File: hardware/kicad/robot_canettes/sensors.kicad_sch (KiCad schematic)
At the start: 5 parts, among them U2 MPU-6050

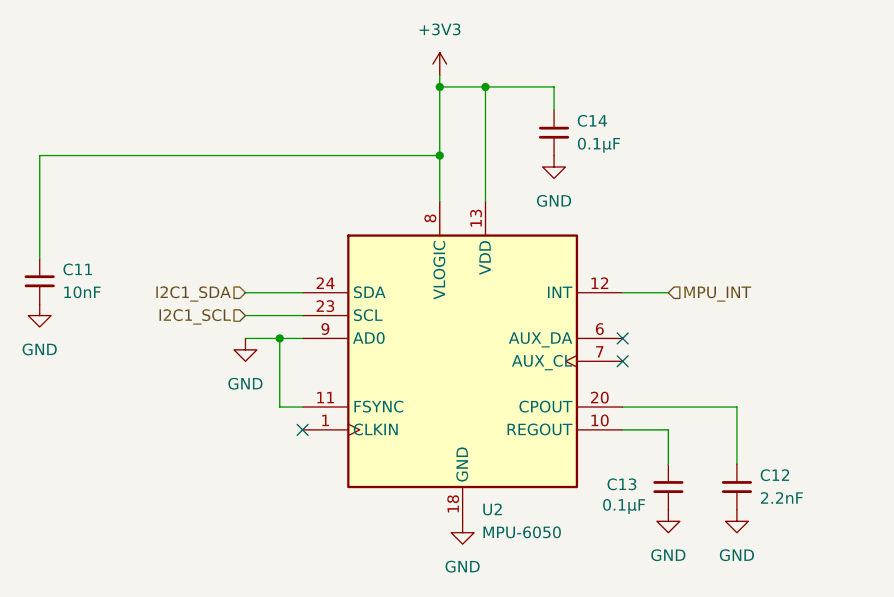
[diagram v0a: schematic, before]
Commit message: MAJ schema MCU/sensors
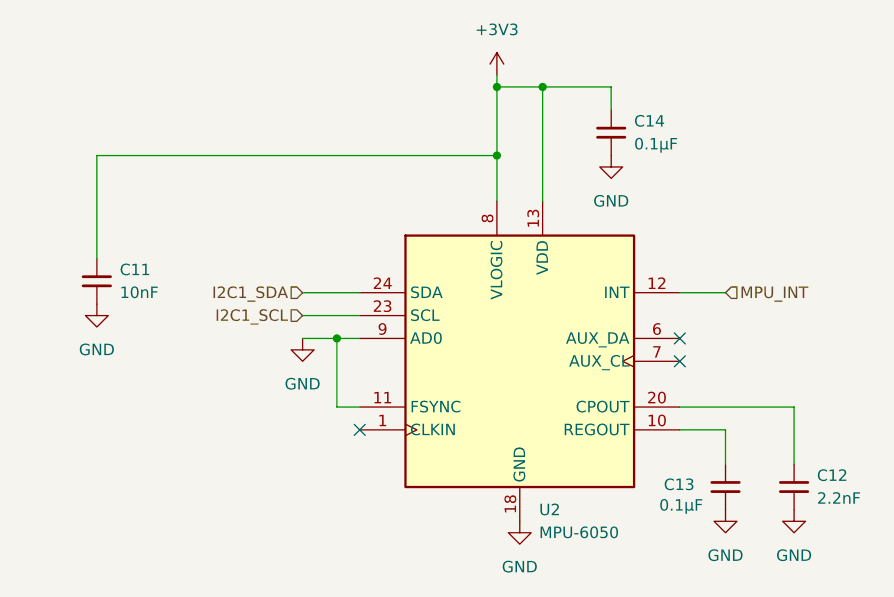
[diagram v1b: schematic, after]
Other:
- moved on the sheet: C11, C12, C13, C14, U2

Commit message: MAJ schema MCU/sensors
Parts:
- C11: JLCPCB PART # (none) -> C15195
- U2: JLCPCB PART # (none) -> C24112
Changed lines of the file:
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@@
+			)
+		)
+		(property "JLCPCB PART #" "C24112"
+			(at 71.12 58.42 0)
+			(hide yes)
+			(show_name no)
+			(do_not_autoplace no)
+			(effects
+				(font
+					(size 1.27 1.27)
+				)
 			)
 		)
@@
 			(hide yes)
 			(show_name no)
+			(do_not_autoplace no)
+			(effects
+				(font
+					(size 1.27 1.27)
+				)
+			)
+		)
+		(property "JLCPCB PART #" "C15195"
+			(at 24.13 49.53 0)
+			(hide yes)
+			(show_name no)

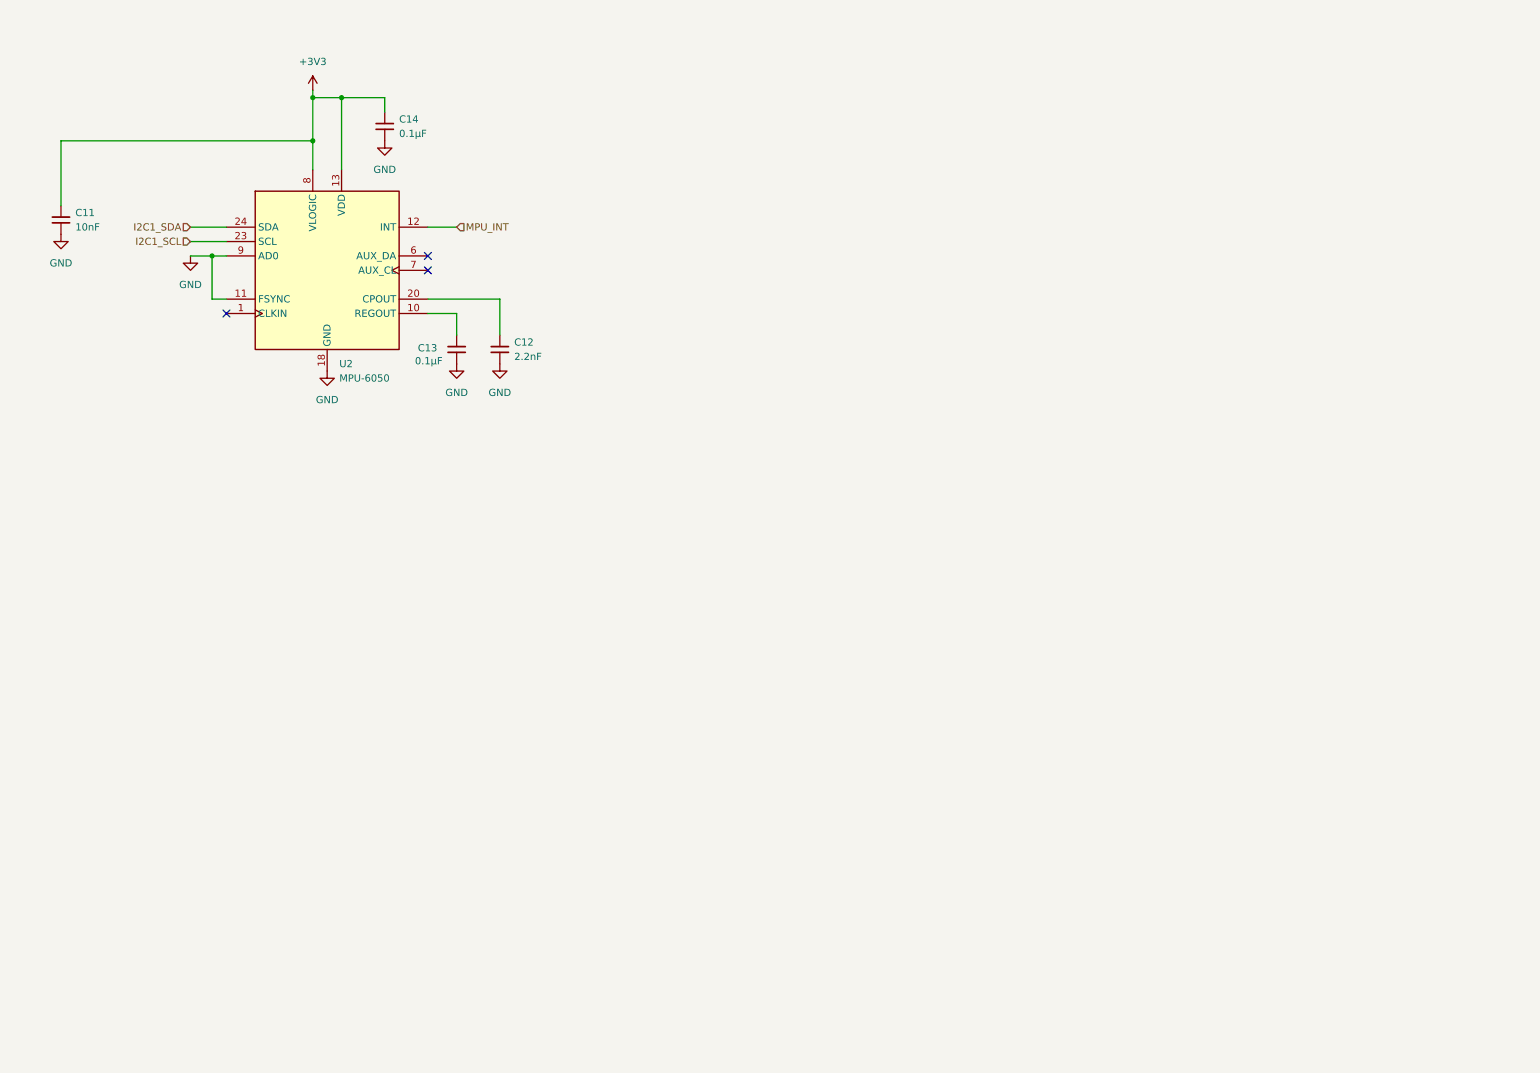
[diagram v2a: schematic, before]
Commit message: MAJ connecteur TOF2 (J10) et resistances pull-up
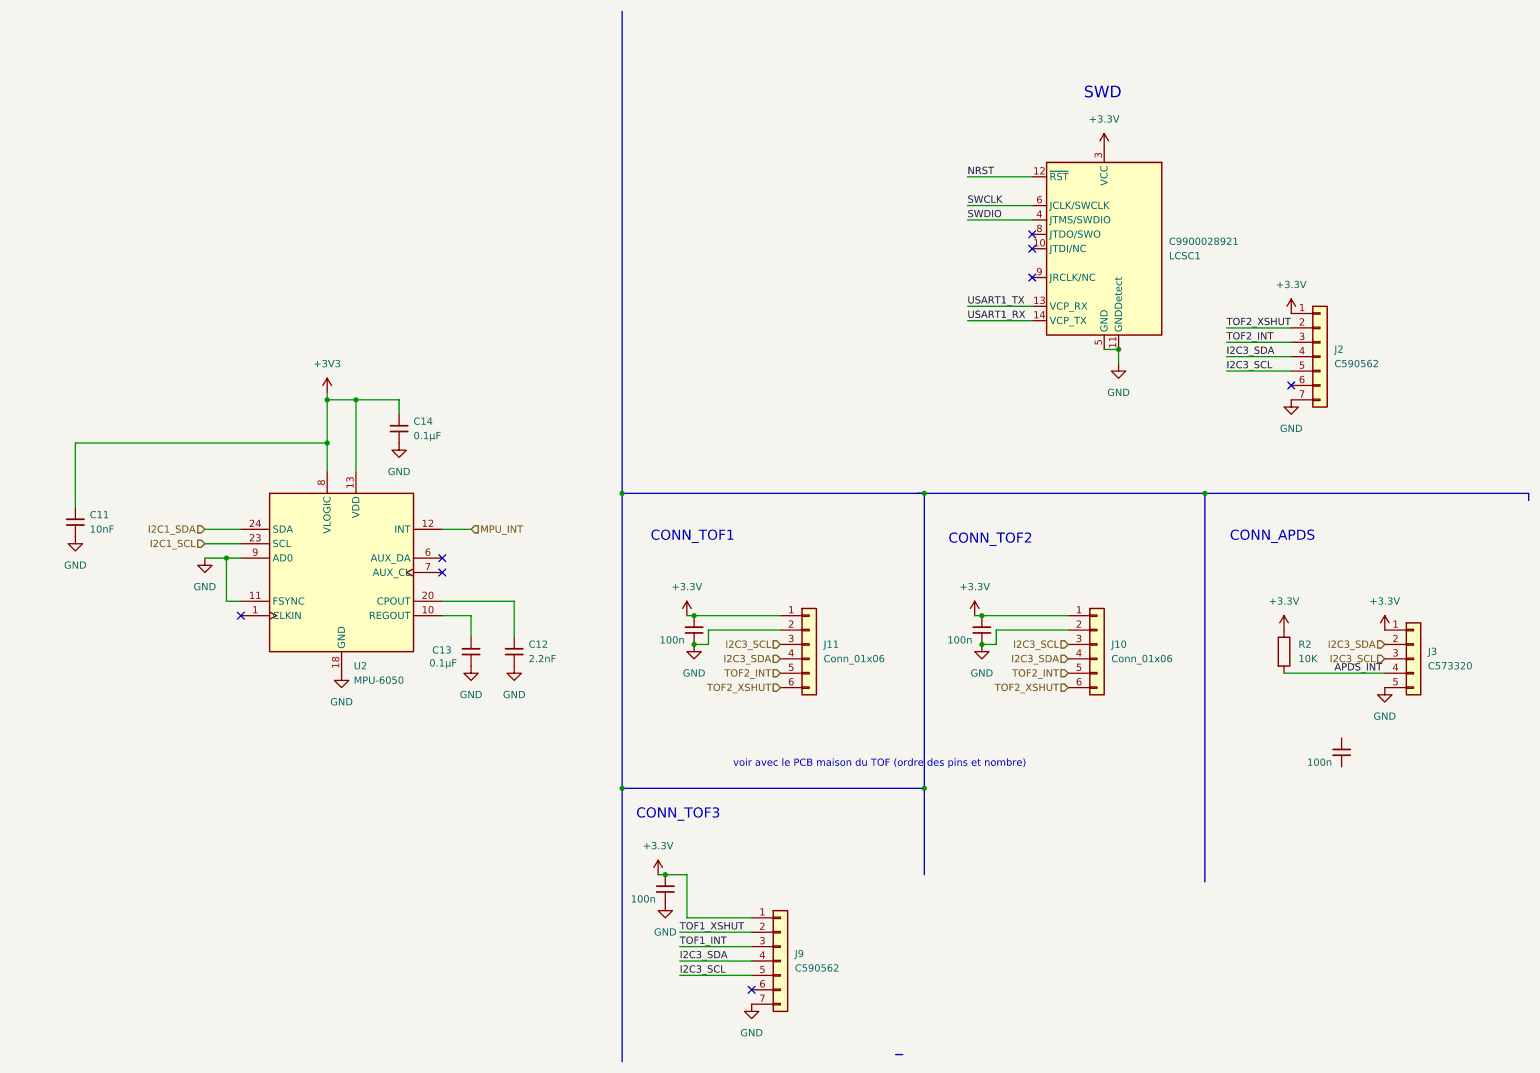
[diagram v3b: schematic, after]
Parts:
- added C36, C38, C39, C40: 100n, symbol Device:C_Small
- added J10, J11: Conn_01x06, symbol Connector_Generic:Conn_01x06
- added J2, J9: C590562, symbol Connector_Generic:Conn_01x07
- added J3: C573320, symbol Connector_Generic:Conn_01x05
- added LCSC1: C9900028921, Package_TO_SOT_SMD:TO-252-2, symbol Connector:Conn_ST_STDC14
- added R2: 10K, symbol Device:R
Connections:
- net GND: now also C36.2, C39.2, C40.2, J10.2 (Pin_2), J11.2 (Pin_2), J2.7 (Pin_7), J3.5 (Pin_5), J9.7 (Pin_7), LCSC1.11 (GNDDetect), LCSC1.5 (GND), LCSC1.7 (GND)
- new net +3.3V: C36.1, C39.1, C40.1, J10.1 (Pin_1), J11.1 (Pin_1), J2.1 (Pin_1), J3.1 (Pin_1), J9.1 (VIN), LCSC1.3 (VCC), R2.1
- new net APDS_INT: J3.4 (Pin_4), R2.2
- new net I2C3_SCL: J10.3 (Pin_3), J11.3 (Pin_3), J2.5 (Pin_5), J3.3 (Pin_3), J9.5 (Pin_5)
- new net I2C3_SDA: J10.4 (Pin_4), J11.4 (Pin_4), J2.4 (Pin_4), J3.2 (Pin_2), J9.4 (Pin_4)
- new net NRST: LCSC1.12 (~{RST})
- new net SWCLK: LCSC1.6 (JCLK/SWCLK)
- new net SWDIO: LCSC1.4 (JTMS/SWDIO)
- new net TOF1_INT: J9.3 (Pin_3)
- new net TOF1_XSHUT: J9.2 (Pin_2)
- new net TOF2_INT: J10.5 (Pin_5), J11.5 (Pin_5), J2.3 (Pin_3)
- new net TOF2_XSHUT: J10.6 (Pin_6), J11.6 (Pin_6), J2.2 (Pin_2)
- new net USART1_RX: LCSC1.14 (VCP_TX)
- new net USART1_TX: LCSC1.13 (VCP_RX)
- no-connect marks 3 -> 8
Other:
- note added: "CONN_APDS"
- note added: "CONN_TOF1"
- note added: "CONN_TOF2"
- note added: "CONN_TOF3"
- note added: "SWD"
- note added: "voir avec le PCB maison du TOF (ordre des pins et nombre)"
- moved on the sheet: C11, C12, C13, C14, U2
